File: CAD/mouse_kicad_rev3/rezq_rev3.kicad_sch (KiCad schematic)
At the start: 99 parts, among them J2 SWD Header, M1 M1_Conn_Alt, M2 M2_Conn_Alt, Q0 TEFT4300, Q1 TEFT4300, Q10 Q_NMOS_GSD, Q11 Q_NMOS_GSD, Q12 Q_NMOS_GSD, Q2 TEFT4300, Q3 TEFT4300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

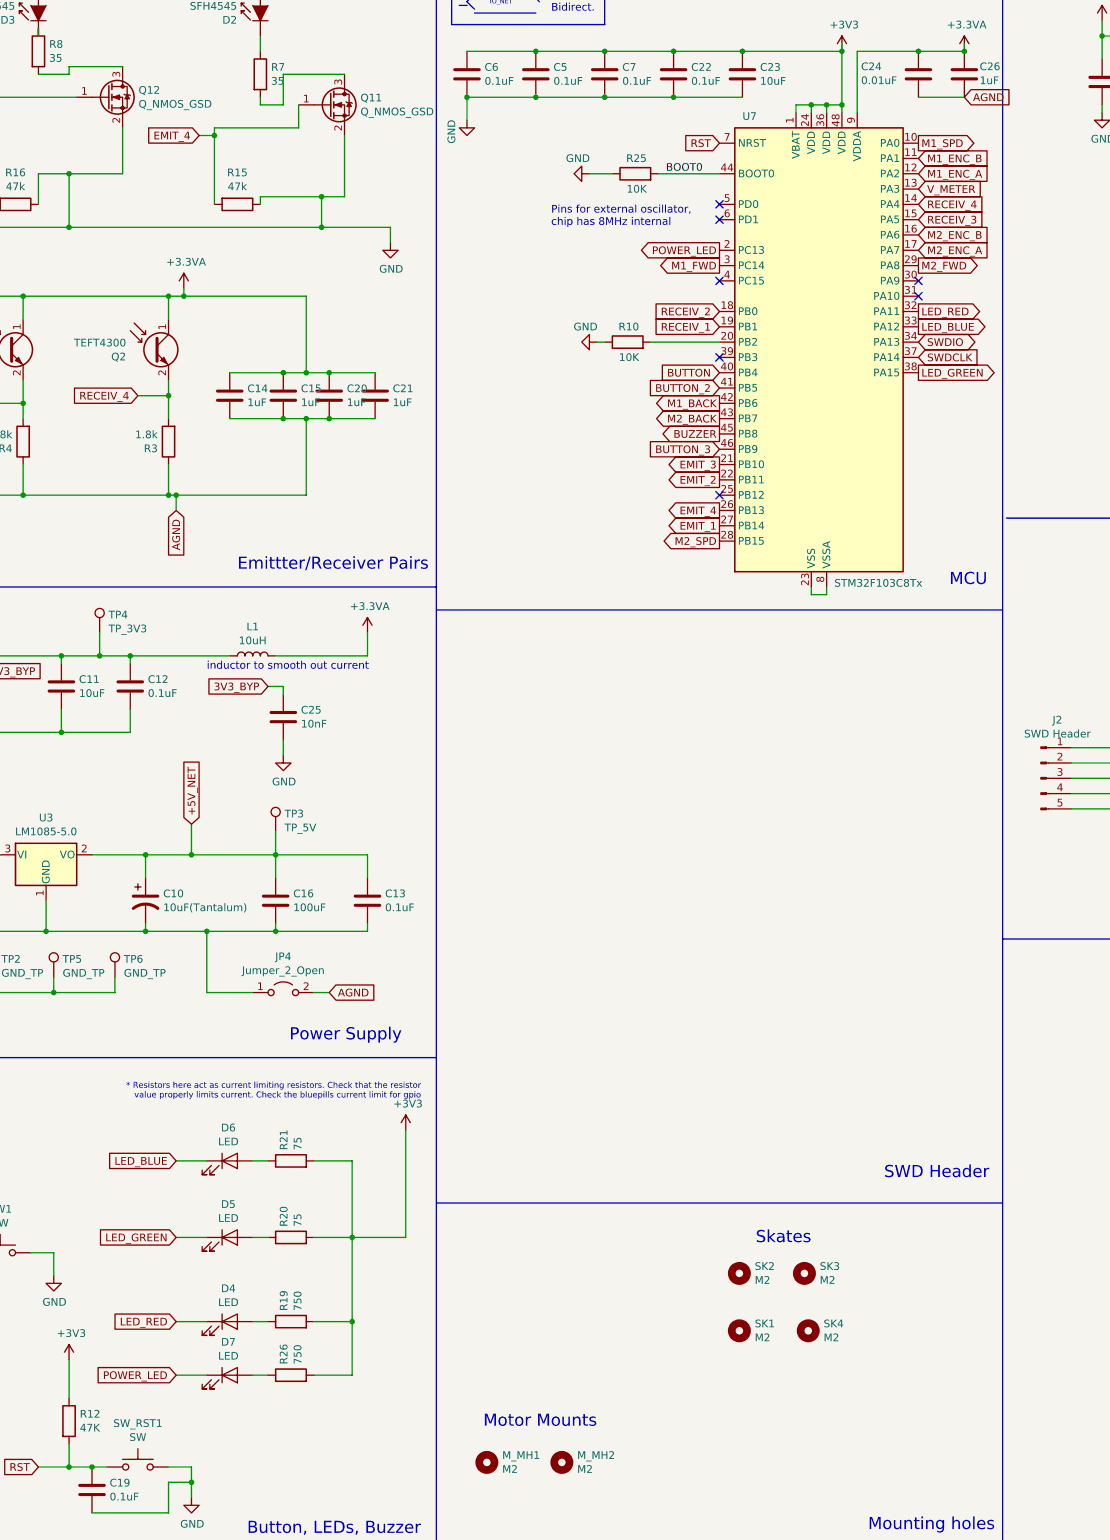
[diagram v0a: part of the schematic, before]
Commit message: Version 3 PCB and some initial test code
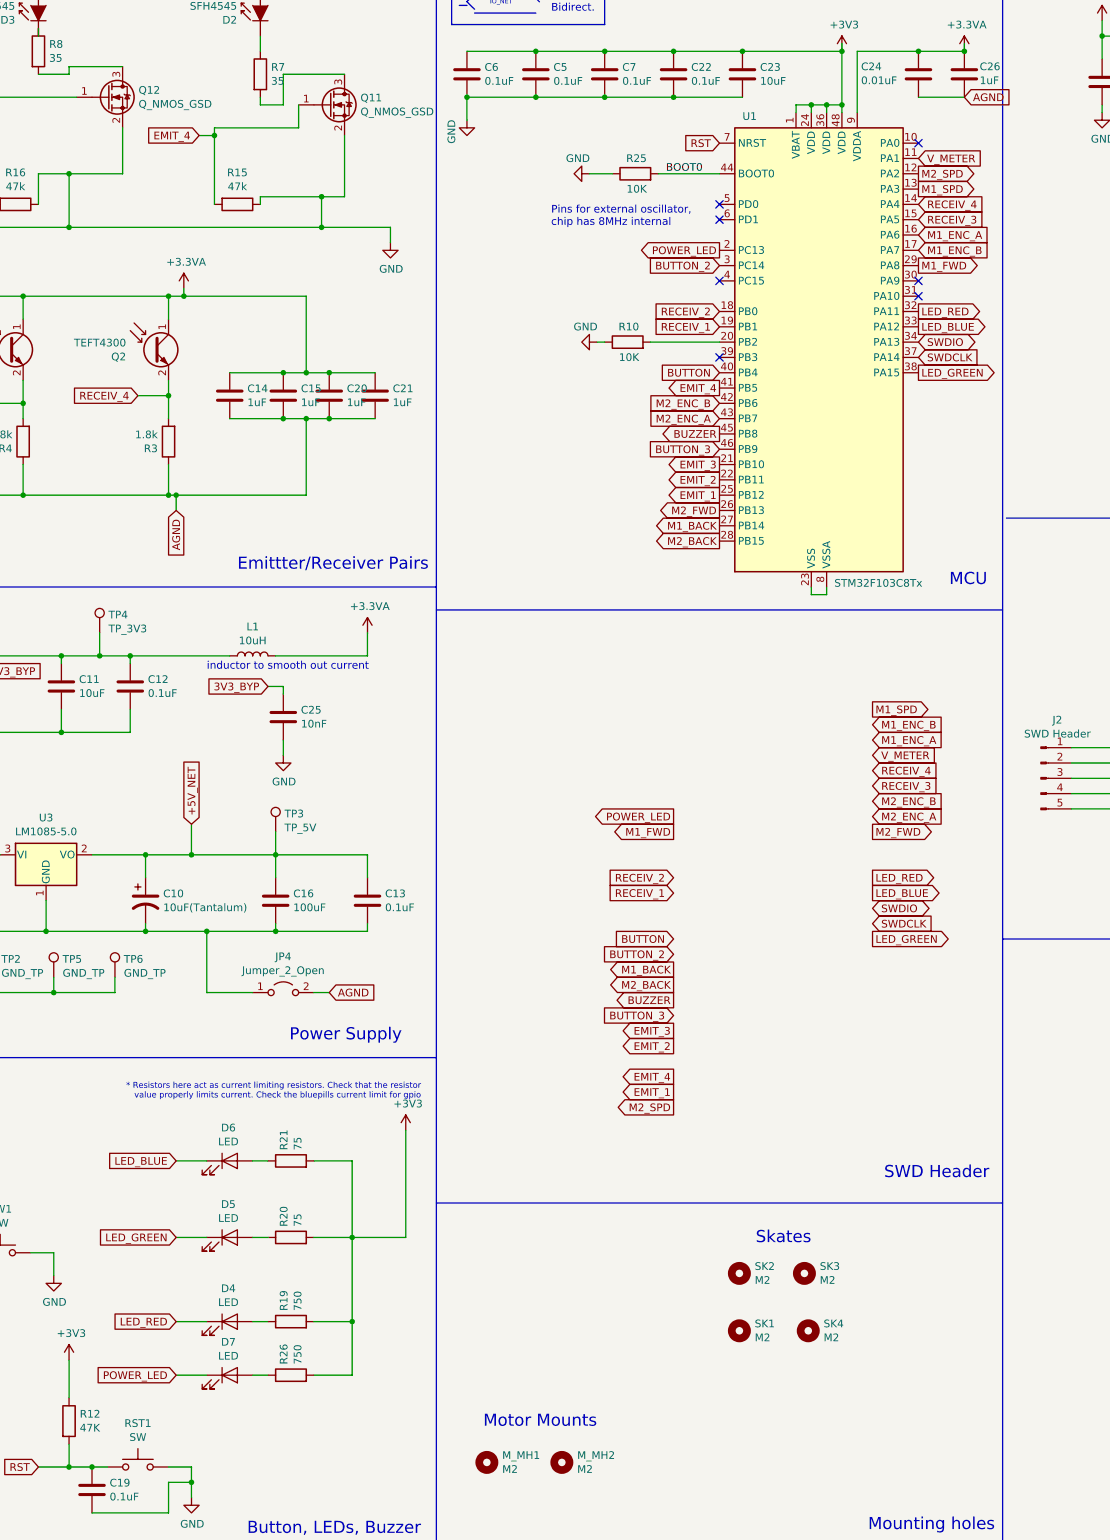
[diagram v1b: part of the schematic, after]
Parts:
- removed U7: STM32F103C8Tx, Package_QFP:LQFP-48_7x7mm_P0.5mm, symbol MCU_ST_STM32F1:STM32F103C8Tx
- added U1: STM32F103C8Tx, Package_QFP:LQFP-48_7x7mm_P0.5mm, symbol MCU_ST_STM32F1:STM32F103C8Tx
- renumbered SW_RST1 to RST1
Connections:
- net +3.3VA: now also U1.9 (VDDA)
- net +3V3: now also U1.1 (VBAT), U1.24 (VDD), U1.36 (VDD), U1.48 (VDD)
- net BOOT0: now also U1.44 (BOOT0)
- net BUTTON: now also U1.40 (PB4)
- net BUTTON_2: now also U1.3 (PC14)
- net BUTTON_3: now also U1.46 (PB9)
- net BUZZER: now also U1.45 (PB8)
- net EMIT_1: now also U1.25 (PB12)
- net EMIT_2: now also U1.22 (PB11)
- net EMIT_3: now also U1.21 (PB10)
- net EMIT_4: now also U1.41 (PB5)
- net LED_BLUE: now also U1.33 (PA12)
- net LED_GREEN: now also U1.38 (PA15)
- net LED_RED: now also U1.32 (PA11)
- net M1_BACK: now also U1.27 (PB14)
- net M1_ENC_A: now also U1.16 (PA6)
- net M1_ENC_B: now also U1.17 (PA7)
- net M1_FWD: now also U1.29 (PA8)
- net M1_SPD: now also U1.13 (PA3)
- net M2_BACK: now also U1.28 (PB15)
- net M2_ENC_A: now also U1.43 (PB7)
- net M2_ENC_B: now also U1.42 (PB6)
- net M2_FWD: now also U1.26 (PB13)
- net M2_SPD: now also U1.12 (PA2)
- net POWER_LED: now also U1.2 (PC13)
- net RECEIV_1: now also U1.19 (PB1)
- net RECEIV_2: now also U1.18 (PB0)
- net RECEIV_3: now also U1.15 (PA5)
- net RECEIV_4: now also U1.14 (PA4)
- net RST: now also U1.7 (NRST)
- net SWDCLK: now also U1.37 (PA14)
- net SWDIO: now also U1.34 (PA13)
- net V_METER: now also U1.11 (PA1)
- net at R10.2: now also U1.20 (PB2)
- new net: U1.23 (VSS), U1.35 (VSS), U1.47 (VSS), U1.8 (VSSA)
